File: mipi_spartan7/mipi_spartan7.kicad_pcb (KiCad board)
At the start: 4 copper layers, 30 x 45 mm, 130 parts, among them J1 SFW15R-1STE1LF, J2 DF40C-60DP-0.4V(51), J3 <DNP> PIN1X2, J4 0878325622, J5 <DNP> SSQ-106-02-F-D-RA, U1 XC7S6-2FTGB196C, U2 IS25LP016D-JULE-TR, U6 AP3401DNTR-G1, U7 AP3401DNTR-G1, U8 TPS22918DBV, X1 SG-210STF 50.0000ML5, X2 SG-210STF 72.0000ML0

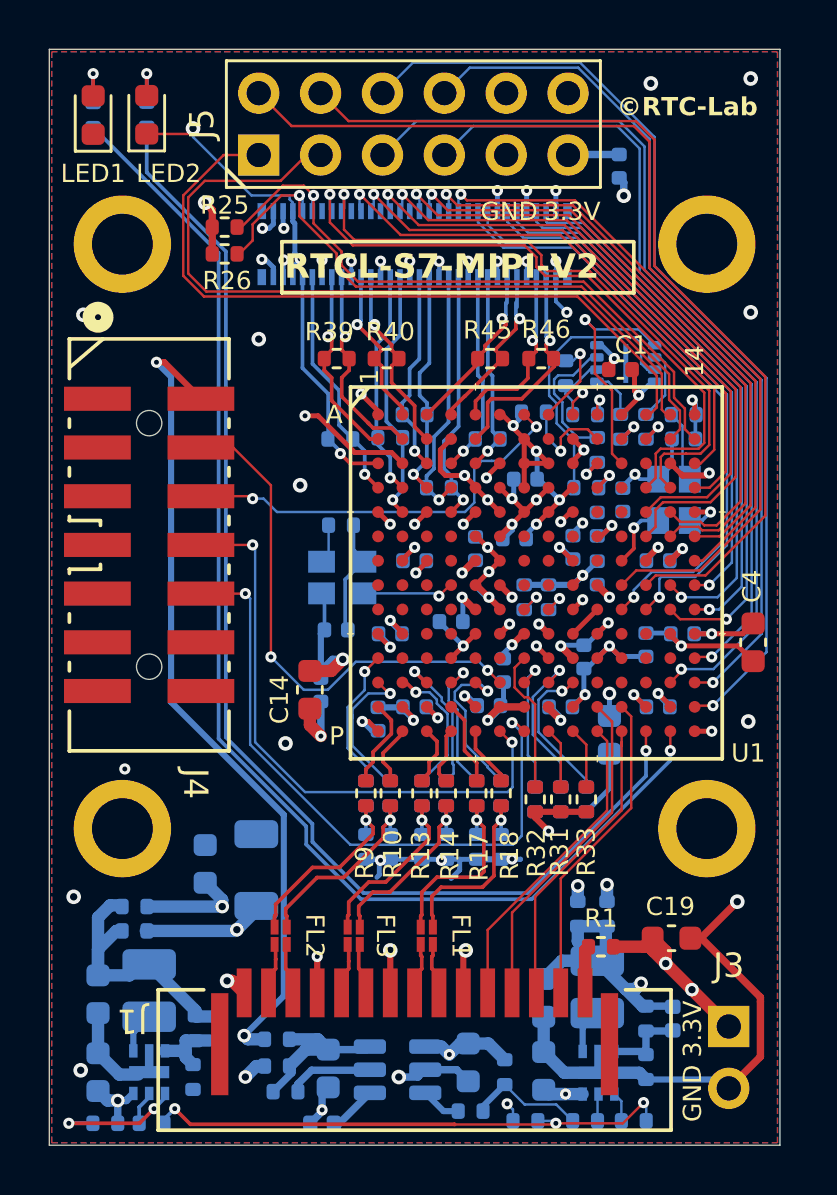
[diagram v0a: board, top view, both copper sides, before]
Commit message: KiCAD 10.0 へ
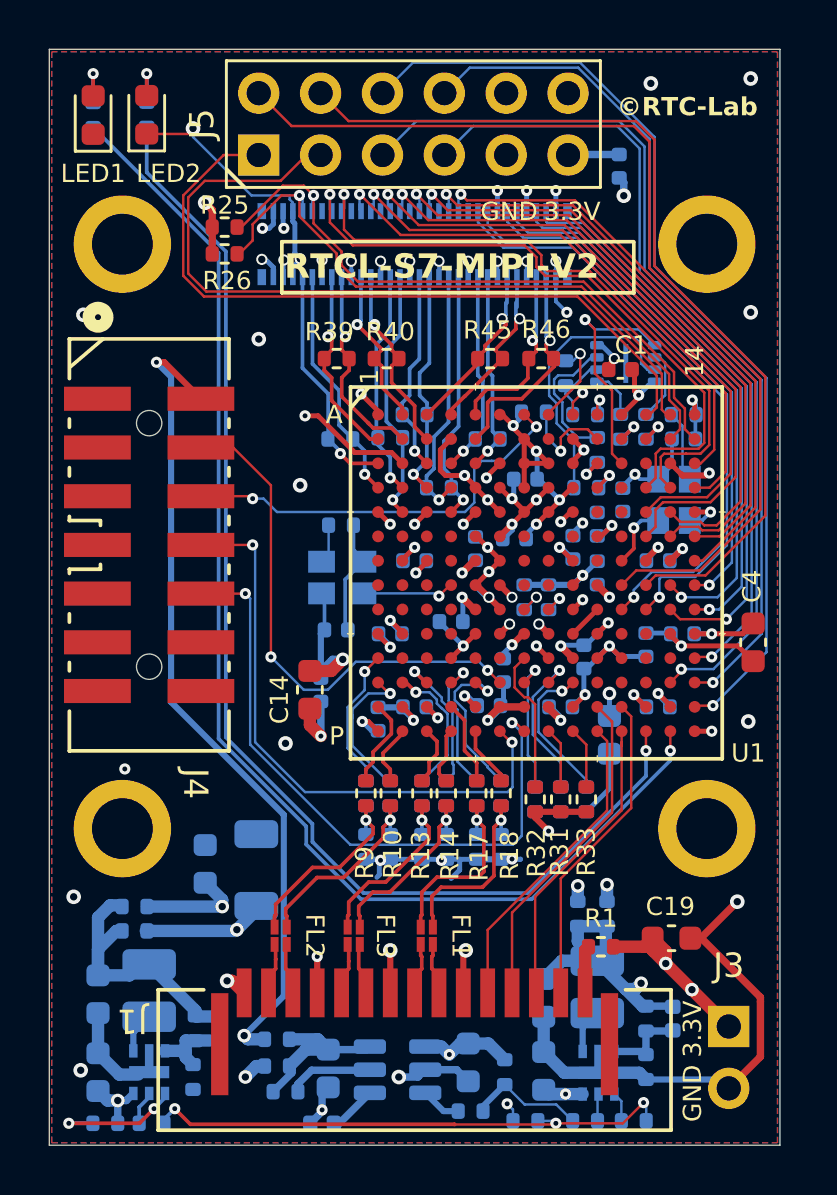
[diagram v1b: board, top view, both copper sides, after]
